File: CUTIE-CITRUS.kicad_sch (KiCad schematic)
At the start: 0 parts

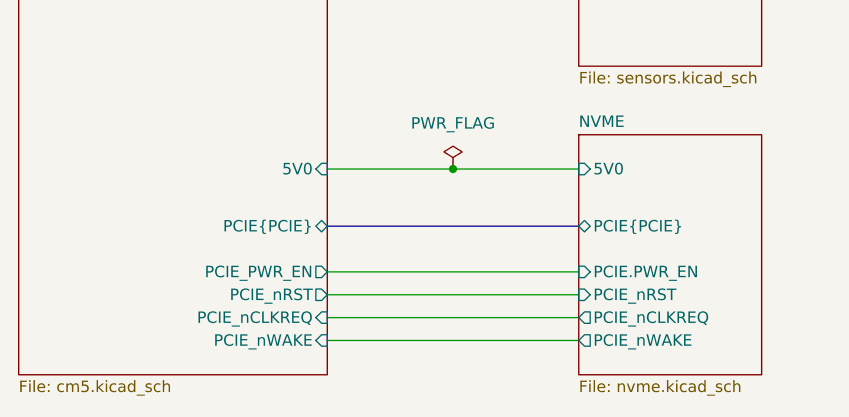
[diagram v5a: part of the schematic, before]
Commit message: abstractified pcie sideband sigs
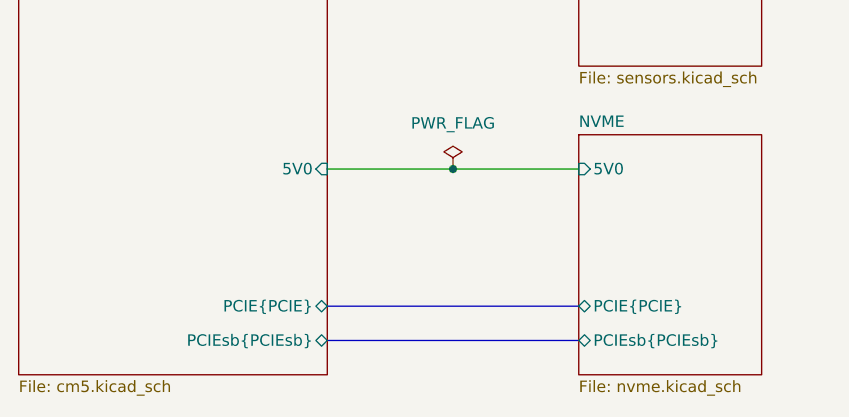
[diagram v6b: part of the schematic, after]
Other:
- sheet CM5 ports: added PCIEsb{PCIEsb}; removed PCIE_PWR_EN, PCIE_nCLKREQ, PCIE_nRST, PCIE_nWAKE
- sheet NVME ports: added PCIEsb{PCIEsb}; removed PCIE.PWR_EN, PCIE_nCLKREQ, PCIE_nRST, PCIE_nWAKE
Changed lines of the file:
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@@
 	(wire
 		(pts
-			(xy 137.16 137.16) (xy 165.1 137.16)
-		)
-		(stroke
-			(width 0)
-			(type default)
-		)
-	)
-	(wire
+			(xy 146.05 86.36) (xy 165.1 86.36)
+		)
+		(stroke
+			(width 0.381)
+			(type default)
+			(color 255 153 0 1)
+		)
+	)
+	(wire
+		(pts
+			(xy 137.16 120.65) (xy 151.13 120.65)
+		)
+		(stroke
+			(width 0.508)
+			(type default)
+			(color 255 0 0 1)
+		)
+	)
+	(bus
+		(pts
+			(xy 137.16 96.52) (xy 165.1 96.52)
+		)
+		(stroke
+			(width 0)
+			(type default)
+		)
+	)
+	(bus
+		(pts
+			(xy 137.16 71.12) (xy 165.1 71.12)
+		)
+		(stroke
+			(width 0)
+			(type default)
+		)
+	)
+	(wire
+		(pts
+			(xy 151.13 44.45) (xy 165.1 44.45)
+		)
+		(stroke
+			(width 0.381)
+			(type default)
+			(color 255 153 0 1)
+		)
+	)
+	(bus
+		(pts
+			(xy 137.16 50.8) (xy 165.1 50.8)
+		)
+		(stroke
+			(width 0)
+			(type default)
+		)
+	)
+	(wire
+		(pts
+			(xy 151.13 120.65) (xy 165.1 120.65)
+		)
+		(stroke
+			(width 0.508)
+			(type default)
+			(color 255 0 0 1)
+		)
+	)
+	(bus
+		(pts
+			(xy 143.51 60.96) (xy 165.1 60.96)
+		)
+		(stroke
+			(width 0)
+			(type default)
+		)
+	)
+	(wire
+		(pts
+			(xy 137.16 54.61) (xy 165.1 54.61)
+		)
+		(stroke
+			(width 0)
+			(type default)
+		)
+	)
+	(bus
 		(pts
 			(xy 137.16 139.7) (xy 165.1 139.7)
@@
 		)
 	)
-	(wire
-		(pts
-			(xy 146.05 86.36) (xy 165.1 86.36)
+	(bus
+		(pts
+			(xy 137.16 60.96) (xy 143.51 60.96)
+		)
+		(stroke
+			(width 0)
+			(type default)
+		)
+	)
+	(bus
+		(pts
+			(xy 143.51 91.44) (xy 143.51 60.96)
+		)
+		(stroke
+			(width 0)
+			(type default)
+		)
+	)
+	(wire
+		(pts
+			(xy 137.16 44.45) (xy 146.05 44.45)
 		)
 		(stroke
@@
 	(wire
 		(pts
-			(xy 137.16 120.65) (xy 151.13 120.65)
-		)
-		(stroke
-			(width 0.508)
-			(type default)
-			(color 255 0 0 1)
-		)
-	)
-	(bus
-		(pts
-			(xy 137.16 96.52) (xy 165.1 96.52)
-		)
-		(stroke
-			(width 0)
-			(type default)
-		)
-	)
-	(bus
-		(pts
-			(xy 137.16 71.12) (xy 165.1 71.12)
-		)
-		(stroke
-			(width 0)
-			(type default)
-		)
-	)
-	(wire
-		(pts
-			(xy 151.13 44.45) (xy 165.1 44.45)
+			(xy 146.05 44.45) (xy 151.13 44.45)
 		)
 		(stroke
@@
 		)
 	)
-	(bus
-		(pts
-			(xy 137.16 50.8) (xy 165.1 50.8)
-		)
-		(stroke
-			(width 0)
-			(type default)
-		)
-	)
-	(wire
-		(pts
-			(xy 151.13 120.65) (xy 165.1 120.65)
-		)
-		(stroke
-			(width 0.508)
-			(type default)
-			(color 255 0 0 1)
-		)
-	)
-	(bus
-		(pts
-			(xy 143.51 60.96) (xy 165.1 60.96)
-		)
-		(stroke
-			(width 0)
-			(type default)
-		)
-	)
-	(wire
-		(pts
-			(xy 137.16 54.61) (xy 165.1 54.61)
-		)
-		(stroke
-			(width 0)
-			(type default)
-		)
-	)
-	(wire
-		(pts
-			(xy 137.16 134.62) (xy 165.1 134.62)
-		)
-		(stroke
-			(width 0)
-			(type default)
-		)
-	)
-	(bus
-		(pts
-			(xy 137.16 60.96) (xy 143.51 60.96)
-		)
-		(stroke
-			(width 0)
-			(type default)
-		)
-	)
-	(bus
-		(pts
-			(xy 143.51 91.44) (xy 143.51 60.96)
-		)
-		(stroke
-			(width 0)
-			(type default)
-		)
-	)
-	(bus
-		(pts
-			(xy 137.16 127) (xy 165.1 127)
-		)
-		(stroke
-			(width 0)
-			(type default)
-		)
-	)
-	(wire
-		(pts
-			(xy 137.16 44.45) (xy 146.05 44.45)
-		)
-		(stroke
-			(width 0.381)
-			(type default)
-			(color 255 153 0 1)
-		)
-	)
-	(wire
-		(pts
-			(xy 146.05 44.45) (xy 151.13 44.45)
-		)
-		(stroke
-			(width 0.381)
-			(type default)
-			(color 255 153 0 1)
-		)
-	)
 	(wire
 		(pts
@@
 		)
 	)
-	(wire
-		(pts
-			(xy 137.16 132.08) (xy 165.1 132.08)
-		)
-		(stroke
-			(width 0)
-			(type default)
-		)
-	)
 	(bus
 		(pts
 			(xy 137.16 67.31) (xy 165.1 67.31)
+		)
+		(stroke
+			(width 0)
+			(type default)
+		)
+	)
+	(bus
+		(pts
+			(xy 137.16 135.89) (xy 165.1 135.89)
 		)
 		(stroke
@@
 			)
 		)
-		(pin "PCIE_nCLKREQ" input
-			(at 137.16 137.16 0)
-			(effects
-				(font
-					(size 1.27 1.27)
-				)
-				(justify right)
-			)
-		)
-		(pin "PCIE_nRST" output
-			(at 137.16 134.62 0)
-			(effects
-				(font
-					(size 1.27 1.27)
-				)
-				(justify right)
-			)
-		)
-		(pin "PCIE_nWAKE" input
-			(at 137.16 139.7 0)
-			(effects
-				(font
-					(size 1.27 1.27)
-				)
-				(justify right)
-			)
-		)
-		(pin "PCIE_PWR_EN" output
-			(at 137.16 132.08 0)
-			(effects
-				(font
-					(size 1.27 1.27)
-				)
-				(justify right)
-			)
-		)
 		(pin "PCIE{PCIE}" bidirectional
-			(at 137.16 127 0)
+			(at 137.16 135.89 0)
 			(effects
 				(font
@@
 		(pin "I2C1{I2C}" bidirectional
 			(at 137.16 71.12 0)
+			(effects
+				(font
+					(size 1.27 1.27)
+				)
+				(justify right)
+			)
+		)
+		(pin "PCIEsb{PCIEsb}" bidirectional
+			(at 137.16 139.7 0)
 			(effects
 				(font
@@
 			)
 		)
-		(pin "PCIE.PWR_EN" input
-			(at 165.1 132.08 180)
-			(effects
-				(font
-					(size 1.27 1.27)
-				)
-				(justify left)
-			)
-		)
-		(pin "PCIE_nCLKREQ" output
-			(at 165.1 137.16 180)
-			(effects
-				(font
-					(size 1.27 1.27)
-				)
-				(justify left)
-			)
-		)
-		(pin "PCIE_nRST" input
-			(at 165.1 134.62 180)
-			(effects
-				(font
-					(size 1.27 1.27)
-				)
-				(justify left)
-			)
-		)
-		(pin "PCIE_nWAKE" output
+		(pin "PCIE{PCIE}" bidirectional
+			(at 165.1 135.89 180)
+			(effects
+				(font
+					(size 1.27 1.27)
+				)
+				(justify left)
+			)
+		)
+		(pin "PCIEsb{PCIEsb}" bidirectional
 			(at 165.1 139.7 180)
 			(effects
 				(font
-					(size 1.27 1.27)
-				)
-				(justify left)
-			)
-		)
-		(pin "PCIE{PCIE}" bidirectional
-			(at 165.1 127 180)
-			(effects
-				(font

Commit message: neo m8m impl.
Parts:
- added 3V3, 5V0, TP1, TP10, TP11, TP12, TP13, TP14, TP15, TP2, TP3, TP4, TP5, TP6, TP7, TP8, TP9: TestPoint, TestPoint:TestPoint_Pad_D1.0mm, symbol Connector:TestPoint
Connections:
- net CM5/3V3: now also 3V3.1
- net CM5/5V0: now also 5V0.1
- new net I2C0.SCL: TP7.1
- new net I2C0.SDA: TP6.1
- new net I2C1.SCL: TP9.1
- new net I2C1.SDA: TP8.1
- new net I2C2.SCL: TP11.1
- new net I2C2.SDA: TP10.1
- new net PCIEsb.PWR_EN: TP14.1
- new net PCIEsb.nCLKREQ: TP12.1
- new net PCIEsb.nRST: TP15.1
- new net PCIEsb.nWAKE: TP13.1
- new net SPI0.CS0n: TP4.1
- new net SPI0.CS1n: TP5.1
- new net SPI0.MISO: TP1.1
- new net SPI0.MOSI: TP2.1
- new net SPI0.SCLK: TP3.1
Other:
- sheet Sensors ports: added I2C2{I2C}; removed I2C0{I2C}

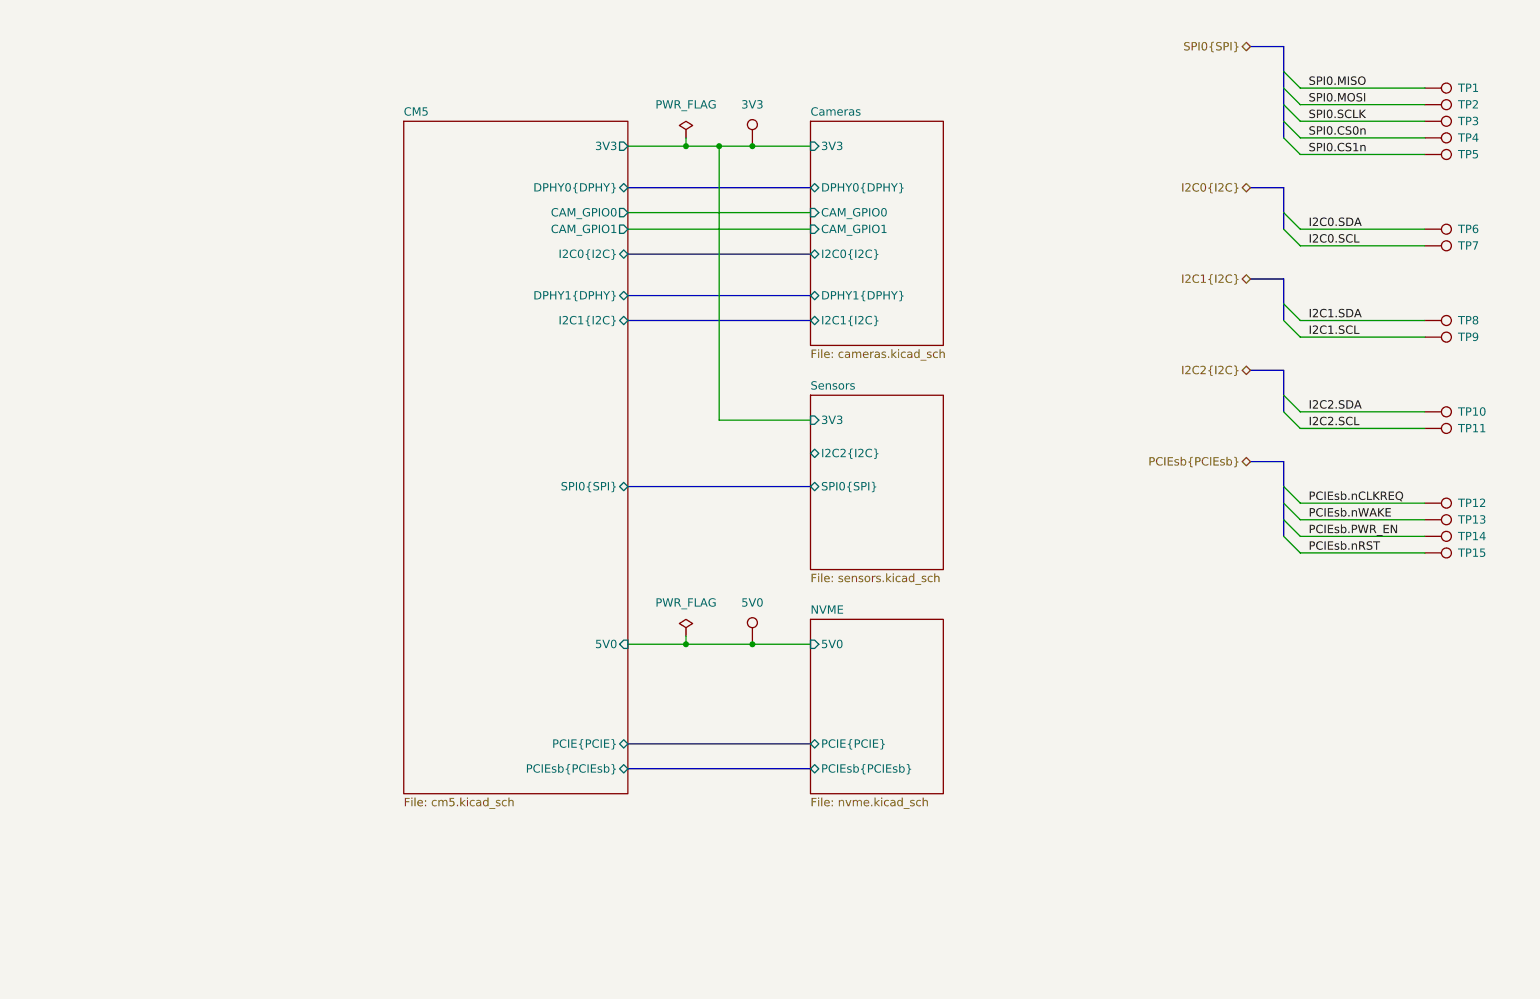
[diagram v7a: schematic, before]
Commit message: prepared usb3, abstracted cameras, backplane connector
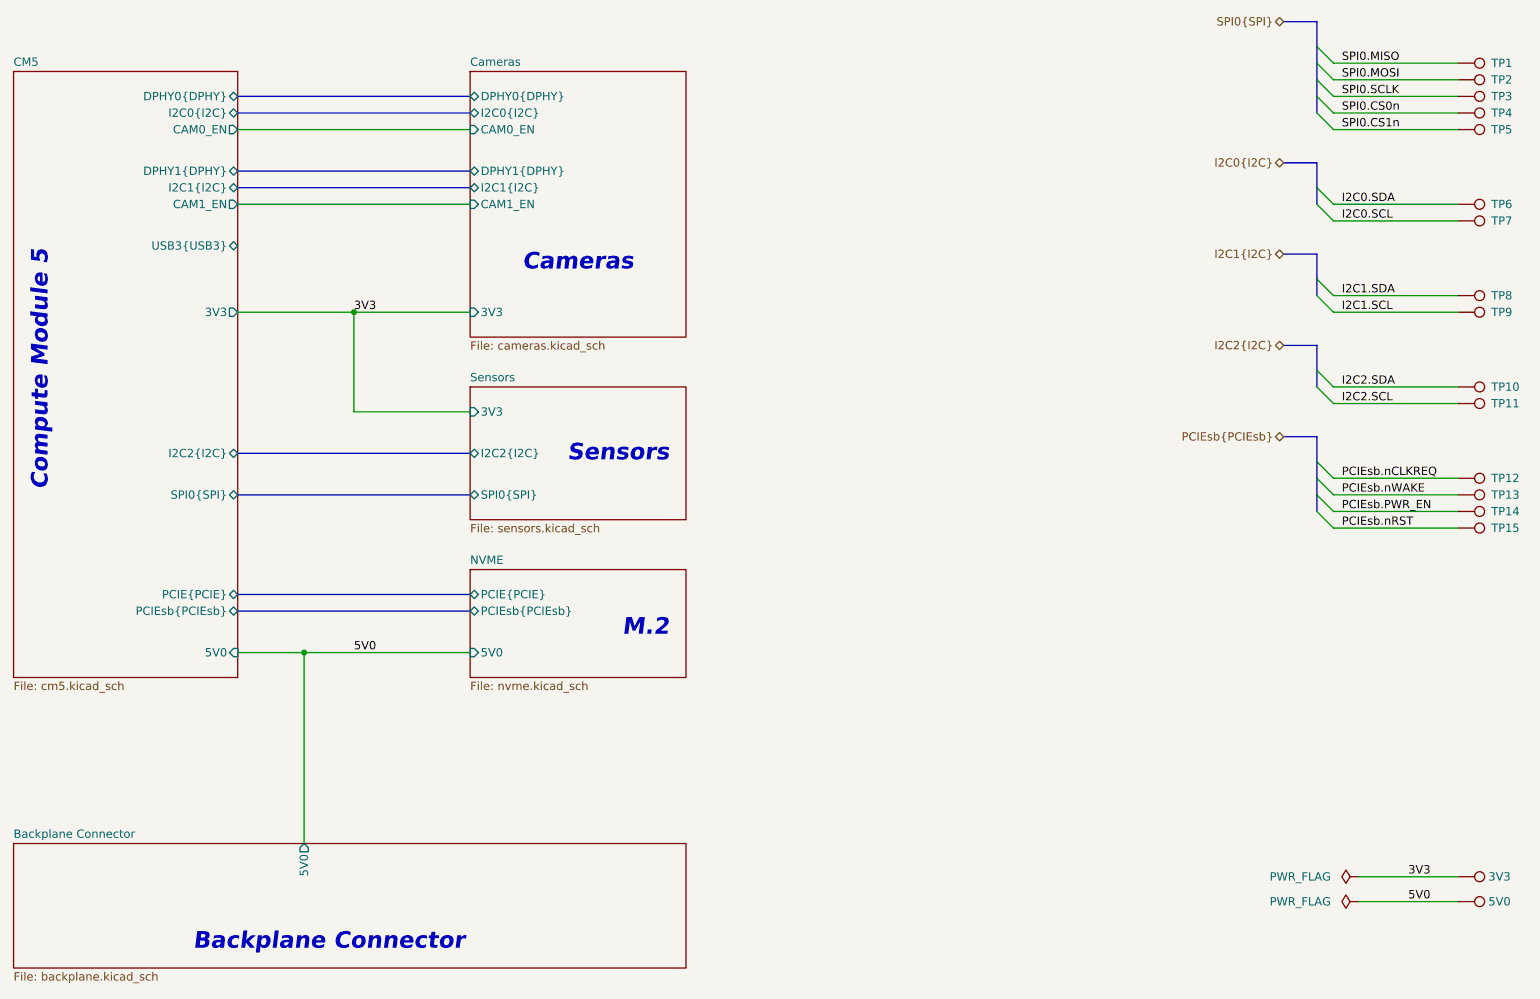
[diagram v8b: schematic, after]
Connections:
- net CM5/3V3 renamed 3V3
- net CM5/5V0 renamed 5V0
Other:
- added sheet Backplane Connector (backplane.kicad_sch)
- sheet CM5 ports: added CAM0_EN, CAM1_EN, I2C2{I2C}, USB3{USB3}; removed CAM_GPIO0, CAM_GPIO1
- sheet Cameras ports: added CAM0_EN, CAM1_EN; removed CAM_GPIO0, CAM_GPIO1
- note added: "Backplane Connector"
- note added: "Cameras"
- note added: "Compute Module 5"
- note added: "M.2"
- note added: "Sensors"
- moved on the sheet: 3V3, 5V0, TP1, TP10, TP11, TP12, TP13, TP14, TP15, TP2, TP3, TP4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
